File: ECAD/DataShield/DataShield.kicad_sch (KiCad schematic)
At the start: 20 parts, among them J1 RS232, J2 Digital, J3 Conn_01x04, J4 Digital, J5 Analog, J6 Communication, U1 SP213, U3 ST485E

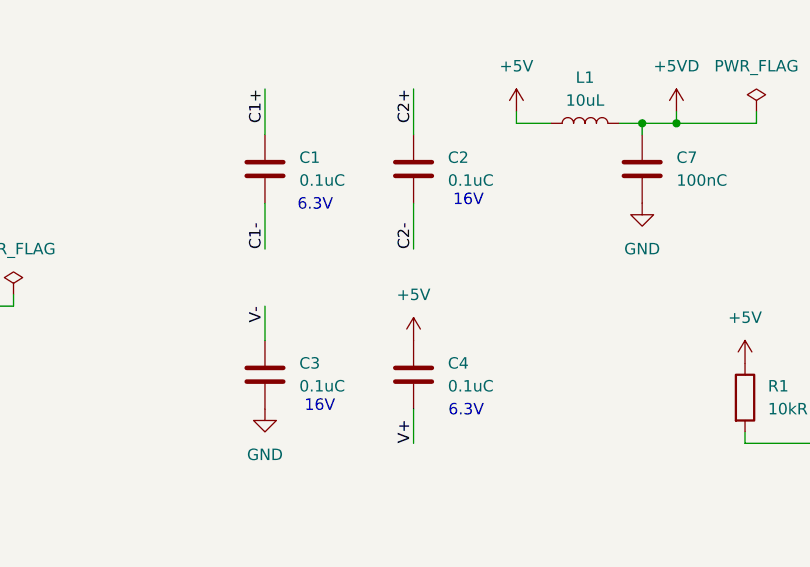
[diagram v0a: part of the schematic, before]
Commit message: Update DataShield.kicad_sch
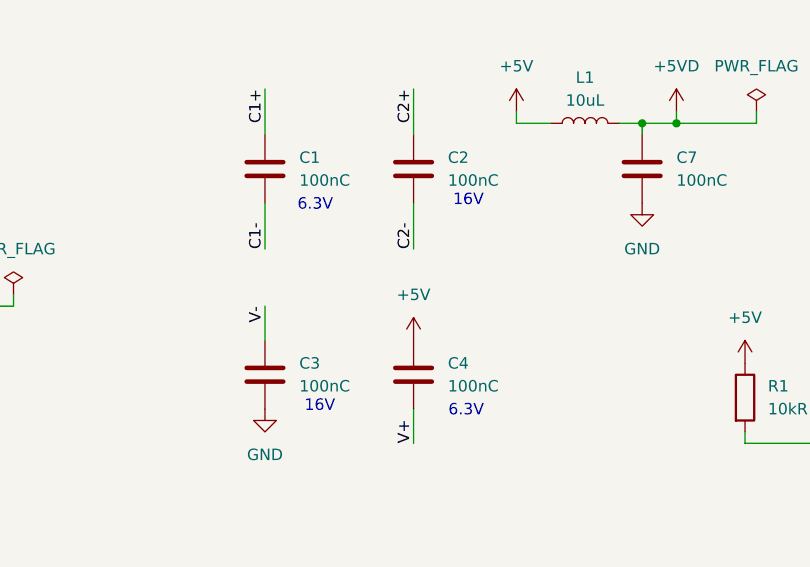
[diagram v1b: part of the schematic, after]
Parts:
- C1, C2, C3, C4: value 0.1uC -> 100nC
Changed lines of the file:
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@@
 			)
 		)
-		(property "Value" "0.1uC"
+		(property "Value" "100nC"
 			(at 123.19 110.4899 0)
 			(effects
@@
 			)
 		)
-		(property "Value" "0.1uC"
+		(property "Value" "100nC"
 			(at 139.7 133.3499 0)
 			(effects
@@
 			)
 		)
-		(property "Value" "0.1uC"
+		(property "Value" "100nC"
 			(at 123.19 133.3499 0)
 			(effects
@@
 			)
 		)
-		(property "Value" "0.1uC"
+		(property "Value" "100nC"
 			(at 139.7 110.4899 0)
 			(effects

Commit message: Progressed ECAD.
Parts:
- C1, C2, C3, C4, C7, C9: MPN (none) -> C0805F104K5RACAUTO; Status (none) -> OK
- R3: value R -> 120R
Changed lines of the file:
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@@
 			)
 		)
-		(property "Value" "R"
+		(property "Value" "120R"
 			(at 226.06 41.9099 0)
 			(effects
@@
 			)
 		)
-		(property "Datasheet" "~"
+		(property "Datasheet" "https://www.lcsc.com/datasheet/lcsc_datasheet_2304140030_KEMET-C0805F104K5RACAUTO_C141162.pdf"
 			(at 161.29 109.22 0)
 			(effects
@@
 			)
 		)
-		(property "Status" ""
+		(property "Status" "OK"
+			(at 161.29 109.22 0)
+			(effects
+				(font
+					(size 1.27 1.27)
+				)
+				(hide yes)
+			)
+		)
+		(property "MPN" "C0805F104K5RACAUTO"
 			(at 161.29 109.22 0)
 			(effects
@@
 			)
 		)
-		(property "Datasheet" "~"
+		(property "Datasheet" "https://www.lcsc.com/datasheet/lcsc_datasheet_2304140030_KEMET-C0805F104K5RACAUTO_C141162.pdf"
 			(at 119.38 109.22 0)
 			(effects
@@
 		)
 		(property "Description" "Unpolarized capacitor"
+			(at 119.38 109.22 0)
+			(effects
+				(font
+					(size 1.27 1.27)
+				)
+				(hide yes)
+			)
+		)
+		(property "MPN" "C0805F104K5RACAUTO"
+			(at 119.38 109.22 0)
+			(effects
+				(font
+					(size 1.27 1.27)
+				)
+				(hide yes)
+			)
+		)
+		(property "Status" "OK"
 			(at 119.38 109.22 0)
 			(effects
@@
 			)
 		)
-		(property "Datasheet" "~"
+		(property "Datasheet" "https://www.lcsc.com/datasheet/lcsc_datasheet_2304140030_KEMET-C0805F104K5RACAUTO_C141162.pdf"
 			(at 135.89 132.08 0)
 			(effects
@@
 		)
 		(property "Description" "Unpolarized capacitor"
+			(at 135.89 132.08 0)
+			(effects
+				(font
+					(size 1.27 1.27)
+				)
+				(hide yes)
+			)
+		)
+		(property "MPN" "C0805F104K5RACAUTO"
+			(at 135.89 132.08 0)
+			(effects
+				(font
+					(size 1.27 1.27)
+				)
+				(hide yes)
+			)
+		)
+		(property "Status" "OK"
 			(at 135.89 132.08 0)
 			(effects
@@
 			)
 		)
-		(property "Datasheet" "~"
+		(property "Datasheet" "https://www.lcsc.com/datasheet/lcsc_datasheet_2304140030_KEMET-C0805F104K5RACAUTO_C141162.pdf"
 			(at 119.38 132.08 0)
 			(effects
@@
 		)
 		(property "Description" "Unpolarized capacitor"
+			(at 119.38 132.08 0)
+			(effects
+				(font
+					(size 1.27 1.27)
+				)
+				(hide yes)
+			)
+		)
+		(property "MPN" "C0805F104K5RACAUTO"
+			(at 119.38 132.08 0)
+			(effects
+				(font
+					(size 1.27 1.27)
+				)
+				(hide yes)
+			)
+		)
+		(property "Status" "OK"
 			(at 119.38 132.08 0)
 			(effects
@@
 			)
 		)
-		(property "Datasheet" "~"
+		(property "Datasheet" "https://www.lcsc.com/datasheet/lcsc_datasheet_2304140030_KEMET-C0805F104K5RACAUTO_C141162.pdf"
 			(at 135.89 109.22 0)
 			(effects
@@
 		)
 		(property "Description" "Unpolarized capacitor"
+			(at 135.89 109.22 0)
+			(effects
+				(font
+					(size 1.27 1.27)
+				)
+				(hide yes)
+			)
+		)
+		(property "MPN" "C0805F104K5RACAUTO"
+			(at 135.89 109.22 0)
+			(effects
+				(font
+					(size 1.27 1.27)
+				)
+				(hide yes)
+			)
+		)
+		(property "Status" "OK"
 			(at 135.89 109.22 0)
 			(effects
@@
 			)
 		)
-		(property "Datasheet" "~"
+		(property "Datasheet" "https://www.lcsc.com/datasheet/lcsc_datasheet_2304140030_KEMET-C0805F104K5RACAUTO_C141162.pdf"
 			(at 161.29 44.45 0)
 			(effects
@@
 			)
 		)
-		(property "Status" ""
+		(property "Status" "OK"
 			(at 161.29 44.45 0)
 			(effects
+				(font
+					(size 1.27 1.27)
+				)
+				(hide yes)
+			)
+		)
+		(property "MPN" "C0805F104K5RACAUTO"
+			(at 161.29 44.45 0)
+			(effects

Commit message: Progressed ECAD.
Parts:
- R1, R2: MPN (none) -> RC0805JR-0710KL; Status (none) -> OK
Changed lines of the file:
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@@
 			)
 		)
-		(property "Datasheet" ""
+		(property "Datasheet" "https://www.lcsc.com/datasheet/lcsc_datasheet_1810171610_YAGEO-RC0805JR-0710KL_C100047.pdf"
 			(at 232.41 134.62 0)
 			(effects
@@
 		)
 		(property "Description" "Resistor"
+			(at 232.41 134.62 0)
+			(effects
+				(font
+					(size 1.27 1.27)
+				)
+				(hide yes)
+			)
+		)
+		(property "MPN" "RC0805JR-0710KL"
+			(at 232.41 134.62 0)
+			(effects
+				(font
+					(size 1.27 1.27)
+				)
+				(hide yes)
+			)
+		)
+		(property "Status" "OK"
 			(at 232.41 134.62 0)
 			(effects
@@
 			)
 		)
-		(property "Datasheet" ""
+		(property "Datasheet" "https://www.lcsc.com/datasheet/lcsc_datasheet_1810171610_YAGEO-RC0805JR-0710KL_C100047.pdf"
 			(at 172.72 134.62 0)
 			(effects
@@
 			(at 172.72 134.62 0)
 			(effects
+				(font
+					(size 1.27 1.27)
+				)
+				(hide yes)
+			)
+		)
+		(property "MPN" "RC0805JR-0710KL"
+			(at 172.72 134.62 0)
+			(effects
+				(font
+					(size 1.27 1.27)
+				)
+				(hide yes)
+			)
+		)
+		(property "Status" "OK"
+			(at 172.72 134.62 0)
+			(effects

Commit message: Progressed ECAD.
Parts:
- removed J3: Conn_01x04, Connector_JST:JST_EH_B4B-EH-A_1x04_P2.50mm_Vertical, symbol Connector_Generic:Conn_01x04
- added J7: Conn_02x03_Odd_Even, Connector_IDC:IDC-Header_2x03_P2.54mm_Vertical, symbol Connector_Generic:Conn_02x03_Odd_Even
- R3: footprint (none) -> Resistor_SMD:R_1206_3216Metric; MPN (none) -> RC1206FR-7W120RL; Status (none) -> OK
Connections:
- net GND: now also J7.3 (Pin_3), J7.4 (Pin_4)
- net at R3.1, U3.6 (A): now also J7.2 (Pin_2)
- net at R3.2, U3.7 (B): now also J7.1 (Pin_1)
- no-connect marks 13 -> 15
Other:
- moved on the sheet: R3

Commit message: Progressed ECAD.
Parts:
- removed R3: 120R, Resistor_SMD:R_1206_3216Metric, symbol Device:R
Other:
- moved on the sheet: J7
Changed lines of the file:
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@@
 	)
 	(junction
-		(at 233.68 48.26)
-		(diameter 0)
-		(color 0 0 0 0)
-	)
-	(junction
 		(at 165.1 104.14)
 		(diameter 0)
@@
 	)
 	(junction
-		(at 233.68 33.02)
-		(diameter 0)
-		(color 0 0 0 0)
-	)
-	(junction
 		(at 83.82 124.46)
 		(diameter 0)
@@
 	)
 	(no_connect
-		(at 250.19 34.29)
+		(at 228.6 34.29)
 	)
 	(no_connect
@@
 	)
 	(no_connect
-		(at 250.19 46.99)
+		(at 228.6 46.99)
 	)
 	(no_connect
@@
 	(wire
 		(pts
-			(xy 219.71 33.02) (xy 233.68 33.02)
-		)
-		(stroke
-			(width 0)
-			(type default)
-		)
-	)
-	(wire
-		(pts
 			(xy 196.85 128.27) (xy 187.96 128.27)
 		)
@@
 	(wire
 		(pts
-			(xy 245.11 48.26) (xy 233.68 48.26)
-		)
-		(stroke
-			(width 0)
-			(type default)
-		)
-	)
-	(wire
-		(pts
 			(xy 184.15 40.64) (xy 196.85 40.64)
 		)
@@
 	(wire
 		(pts
-			(xy 219.71 48.26) (xy 233.68 48.26)
+			(xy 219.71 48.26) (xy 223.52 48.26)
 		)
 		(stroke
@@
 	(wire
 		(pts
-			(xy 245.11 33.02) (xy 233.68 33.02)
+			(xy 219.71 33.02) (xy 223.52 33.02)
 		)
 		(stroke
@@
 	(wire
 		(pts
-			(xy 245.11 34.29) (xy 245.11 33.02)
+			(xy 223.52 34.29) (xy 223.52 33.02)
 		)
 		(stroke
@@
 	(wire
 		(pts
-			(xy 245.11 46.99) (xy 245.11 48.26)
+			(xy 223.52 46.99) (xy 223.52 48.26)
 		)
 		(stroke
@@
 	(wire
 		(pts
-			(xy 233.68 33.02) (xy 233.68 36.83)
-		)
-		(stroke
-			(width 0)
-			(type default)
-		)
-	)
-	(wire
-		(pts
 			(xy 196.85 133.35) (xy 187.96 133.35)
 		)
@@
 	(wire
 		(pts
-			(xy 233.68 44.45) (xy 233.68 48.26)
-		)
-		(stroke
-			(width 0)
-			(type default)
-		)
-	)
-	(wire
-		(pts
 			(xy 147.32 39.37) (xy 151.13 39.37)
 		)
@@
 	)
 	(symbol
-		(lib_id "Device:R")
-		(at 233.68 40.64 0)
-		(unit 1)
-		(exclude_from_sim no)
-		(in_bom yes)
-		(on_board yes)
-		(dnp no)
-		(fields_autoplaced yes)
-		(property "Reference" "R3"
-			(at 236.22 39.3699 0)
-			(effects
-				(font
-					(size 1.27 1.27)
-				)
-				(justify left)
-			)
-		)
-		(property "Value" "120R"
-			(at 236.22 41.9099 0)
-			(effects
-				(font
-					(size 1.27 1.27)
-				)
-				(justify left)
-			)
-		)
-		(property "Footprint" "Resistor_SMD:R_1206_3216Metric"
-			(at 231.902 40.64 90)
-			(effects
-				(font
-					(size 1.27 1.27)
-				)
-				(hide yes)
-			)
-		)
-		(property "Datasheet" "https://www.lcsc.com/datasheet/lcsc_datasheet_2011202108_YAGEO-RC1206FR-7W120RL_C914848.pdf"
-			(at 233.68 40.64 0)
-			(effects
-				(font
-					(size 1.27 1.27)
-				)
-				(hide yes)
-			)
-		)
-		(property "Description" "Resistor"
-			(at 233.68 40.64 0)
-			(effects
-				(font
-					(size 1.27 1.27)
-				)
-				(hide yes)
-			)
-		)
-		(property "MPN" "RC1206FR-7W120RL"
-			(at 233.68 40.64 0)
-			(effects
-				(font
-					(size 1.27 1.27)
-				)
-				(hide yes)
-			)
-		)
-		(property "Status" "OK"
-			(at 233.68 40.64 0)
-			(effects
-				(font
-					(size 1.27 1.27)
-				)
-				(hide yes)
-			)
-		)
-		(pin "2"
-		)
-		(pin "1"
-		)
-		(instances
-			(project "DataShield"
-				(path "/e63e39d7-6ac0-4ffd-8aa3-1841a4541b55"
-					(reference "R3")
-					(unit 1)
-				)
-			)
-		)
-	)
-	(symbol
 		(lib_id "Connector_Generic:Conn_01x02")
 		(at 35.56 135.89 0)
@@
 		(lib_name "GND_2")
 		(lib_id "power:GND")
-		(at 247.65 46.99 0)
+		(at 226.06 46.99 0)
 		(unit 1)
 		(exclude_from_sim no)
@@
 		(fields_autoplaced yes)
 		(property "Reference" "#PWR019"
-			(at 247.65 53.34 0)
+			(at 226.06 53.34 0)
 			(effects
 				(font
@@
 		)
 		(property "Value" "GND"
-			(at 247.65 52.07 0)
+			(at 226.06 52.07 0)
 			(effects
 				(font
@@
 		)
 		(property "Footprint" ""
-			(at 247.65 46.99 0)
+			(at 226.06 46.99 0)
 			(effects
 				(font
@@
 		)
 		(property "Datasheet" ""
-			(at 247.65 46.99 0)
+			(at 226.06 46.99 0)
 			(effects
 				(font
@@
 		)
 		(property "Description" "Power symbol creates a global label with name \"GND\" , ground"
-			(at 247.65 46.99 0)
+			(at 226.06 46.99 0)
 			(effects
 				(font
@@
 	(symbol
 		(lib_id "Connector_Generic:Conn_02x03_Odd_Even")
-		(at 247.65 41.91 90)
+		(at 226.06 41.91 90)
 		(unit 1)
 		(exclude_from_sim no)
@@
 		(fields_autoplaced yes)
 		(property "Reference" "J7"
-			(at 252.73 39.3699 90)
+			(at 231.14 39.3699 90)
 			(effects
 				(font
@@
 		)
 		(property "Value" "Conn_02x03_Odd_Even"
-			(at 252.73 41.9099 90)
+			(at 231.14 41.9099 90)
 			(effects
 				(font
@@
 		)
 		(property "Footprint" "Connector_IDC:IDC-Header_2x03_P2.54mm_Vertical"
-			(at 247.65 41.91 0)
+			(at 226.06 41.91 0)
 			(effects
 				(font
@@
 		)
 		(property "Datasheet" "https://www.lcsc.com/datasheet/lcsc_datasheet_2303141000_HCTL-HC-JN254-2-03-Z_C5372863.pdf"
-			(at 247.65 41.91 0)
+			(at 226.06 41.91 0)
 			(effects
 				(font
@@
 		)
 		(property "Description" "Generic connector, double row, 02x03, odd/even pin numbering scheme (row 1 odd numbers, row 2 even numbers), script generated (kicad-library-utils/schlib/autogen/connector/)"
-			(at 247.65 41.91 0)
+			(at 226.06 41.91 0)
 			(effects
 				(font
@@
 		)
 		(property "MPN" "HC-JN254-2-03-Z"
-			(at 247.65 41.91 0)
+			(at 226.06 41.91 0)
 			(effects
 				(font
@@
 		)
 		(property "Status" "OK"
-			(at 247.65 41.91 0)
+			(at 226.06 41.91 0)
 			(effects
 				(font
@@
 		(lib_name "GND_2")
 		(lib_id "power:GND")
-		(at 247.65 34.29 180)
+		(at 226.06 34.29 180)
 		(unit 1)
 		(exclude_from_sim no)
@@
 		(fields_autoplaced yes)
 		(property "Reference" "#PWR08"
-			(at 247.65 27.94 0)
+			(at 226.06 27.94 0)
 			(effects
 				(font
@@
 		)
 		(property "Value" "GND"
-			(at 247.65 29.21 0)
+			(at 226.06 29.21 0)
 			(effects
 				(font
@@
 		)
 		(property "Footprint" ""
-			(at 247.65 34.29 0)
+			(at 226.06 34.29 0)
 			(effects
 				(font
@@
 		)
 		(property "Datasheet" ""
-			(at 247.65 34.29 0)
+			(at 226.06 34.29 0)
 			(effects
 				(font
@@
 		)
 		(property "Description" "Power symbol creates a global label with name \"GND\" , ground"
-			(at 247.65 34.29 0)
+			(at 226.06 34.29 0)
 			(effects
 				(font

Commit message: Progressed ECAD.
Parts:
- removed C8: 100uC, Capacitor_SMD:CP_Elec_6.3x5.4_Nichicon, symbol Device:C_Polarized
- added C5: 10uC, Capacitor_SMD:C_1206_3216Metric, symbol Device:C
- added J3: Wire RS485, Connector_IDC:IDC-Header_2x03_P2.54mm_Vertical, symbol Connector_Generic:Conn_02x03_Odd_Even
- J7: value Conn_02x03_Odd_Even -> RS485
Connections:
- net +5V: now also C5.1
- net GND: now also C5.2

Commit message: Progressed ECAD.
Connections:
- net 22: no longer U1.5 (ROUT2)
- net 23: no longer U1.26 (ROUT3)
- net 24: no longer U1.22 (ROUT4)
- net 25: no longer U1.19 (ROUT5)
- net A12: now also U1.5 (ROUT2)
- net A13: now also U1.26 (ROUT3)
- net A14: now also U1.22 (ROUT4)
- net A15: now also U1.19 (ROUT5)
- no-connect marks 15 -> 21
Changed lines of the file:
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@@
 	)
 	(no_connect
-		(at 29.21 64.77)
+		(at 76.2 120.65)
 	)
 	(no_connect
@@
 	)
 	(no_connect
+		(at 245.11 46.99)
+	)
+	(no_connect
 		(at 85.09 69.85)
 	)
 	(no_connect
+		(at 247.65 34.29)
+	)
+	(no_connect
+		(at 73.66 153.67)
+	)
+	(no_connect
 		(at 228.6 46.99)
 	)
@@
 	)
 	(no_connect
-		(at 29.21 72.39)
+		(at 76.2 153.67)
+	)
+	(no_connect
+		(at 247.65 46.99)
 	)
 	(no_connect
@@
 	)
 	(no_connect
-		(at 29.21 67.31)
+		(at 242.57 34.29)
+	)
+	(no_connect
+		(at 245.11 34.29)
 	)
 	(no_connect
@@
 	)
 	(no_connect
-		(at 29.21 69.85)
+		(at 242.57 46.99)
+	)
+	(no_connect
+		(at 73.66 120.65)
 	)
 	(no_connect
@@
 	(wire
 		(pts
+			(xy 30.48 64.77) (xy 43.18 64.77)
+		)
+		(stroke
+			(width 0)
+			(type default)
+		)
+	)
+	(wire
+		(pts
 			(xy 71.12 59.69) (xy 83.82 59.69)
 		)
@@
 	(wire
 		(pts
-			(xy 29.21 72.39) (xy 43.18 72.39)
-		)
-		(stroke
-			(width 0)
-			(type solid)
-		)
-	)
-	(wire
-		(pts
 			(xy 83.82 123.19) (xy 83.82 124.46)
 		)
@@
 	(wire
 		(pts
-			(xy 43.18 69.85) (xy 29.21 69.85)
+			(xy 29.21 133.35) (xy 29.21 135.89)
 		)
 		(stroke
 			(width 0)
-			(type solid)
+			(type default)
 		)
 	)
 	(wire
 		(pts
-			(xy 29.21 133.35) (xy 29.21 135.89)
+			(xy 29.21 135.89) (xy 29.21 138.43)
 		)
 		(stroke
@@
 	(wire
 		(pts
-			(xy 29.21 135.89) (xy 29.21 138.43)
+			(xy 184.15 45.72) (xy 196.85 45.72)
 		)
 		(stroke
 			(width 0)
-			(type default)
+			(type solid)
 		)
 	)
 	(wire
 		(pts
-			(xy 184.15 45.72) (xy 196.85 45.72)
+			(xy 71.12 67.31) (xy 83.82 67.31)
 		)
 		(stroke
@@
 	(wire
 		(pts
-			(xy 71.12 67.31) (xy 83.82 67.31)
+			(xy 30.48 69.85) (xy 43.18 69.85)
 		)
 		(stroke
 			(width 0)
-			(type solid)
+			(type default)
 		)
 	)
@@
 	(wire
 		(pts
+			(xy 30.48 67.31) (xy 43.18 67.31)
+		)
+		(stroke
+			(width 0)
+			(type default)
+		)
+	)
+	(wire
+		(pts
 			(xy 196.85 135.89) (xy 187.96 135.89)
 		)
@@
 	(wire
 		(pts
-			(xy 29.21 67.31) (xy 43.18 67.31)
-		)
-		(stroke
-			(width 0)
-			(type solid)
-		)
-	)
-	(wire
-		(pts
 			(xy 219.71 33.02) (xy 219.71 38.1)
 		)
@@
 	(wire
 		(pts
-			(xy 147.32 39.37) (xy 151.13 39.37)
+			(xy 30.48 72.39) (xy 43.18 72.39)
 		)
 		(stroke
@@
 	(wire
 		(pts
-			(xy 196.85 119.38) (xy 187.96 119.38)
+			(xy 147.32 39.37) (xy 151.13 39.37)
 		)
 		(stroke
 			(width 0)
-			(type solid)
+			(type default)
 		)
 	)
 	(wire
 		(pts
-			(xy 184.15 50.8) (xy 196.85 50.8)
+			(xy 196.85 119.38) (xy 187.96 119.38)
 		)
 		(stroke
@@
 	(wire
 		(pts
-			(xy 43.18 64.77) (xy 29.21 64.77)
+			(xy 184.15 50.8) (xy 196.85 50.8)
 		)
 		(stroke
@@
 		)
 	)
-	(label "RX2{slash}17"
-		(at 184.15 40.64 0)
+	(label "A14"
+		(at 187.96 133.35 0)
 		(fields_autoplaced yes)
 		(effects
@@
 		)
 	)
-	(label "25"
-		(at 73.66 153.67 90)
+	(label "RX2{slash}17"
+		(at 184.15 40.64 0)
 		(fields_autoplaced yes)
 		(effects
@@
 		)
 	)
-	(label "DCD"
-		(at 248.92 109.22 0)
+	(label "25"
+		(at 73.66 153.67 90)
 		(fields_autoplaced yes)
 		(effects
@@
 		)
 	)
-	(label "22"
-		(at 187.96 128.27 0)
+	(label "DCD"
+		(at 248.92 109.22 0)
 		(fields_autoplaced yes)
 		(effects
@@
 		)
 	)
+	(label "A12"
+		(at 187.96 128.27 0)
+		(fields_autoplaced yes)
+		(effects
+			(font
+				(size 1.27 1.27)
+			)
+			(justify left bottom)
+		)
+	)
 	(label "23"
 		(at 76.2 153.67 90)
@@
 		)
 	)
-	(label "TX1{slash}18"
-		(at 184.15 43.18 0)
+	(label "A13"
+		(at 187.96 130.81 0)
 		(fields_autoplaced yes)
 		(effects
@@
 		)
 	)
-	(label "23"
-		(at 187.96 130.81 0)
+	(label "TX1{slash}18"
+		(at 184.15 43.18 0)
 		(fields_autoplaced yes)
 		(effects
@@
 		)
 	)
+	(label "A15"
+		(at 187.96 135.89 0)
+		(fields_autoplaced yes)
+		(effects
+			(font
+				(size 1.27 1.27)
+			)
+			(justify left bottom)
+		)
+	)
 	(label "RX1{slash}19"
 		(at 83.82 67.31 180)
@@
 		)
 	)
-	(label "24"
-		(at 187.96 133.35 0)
-		(fields_autoplaced yes)
-		(effects
-			(font
-				(size 1.27 1.27)
-			)
-			(justify left bottom)
-		)
-	)
 	(label "RI"
 		(at 248.92 127 0)
@@
 		)
 	)
-	(label "25"
-		(at 187.96 135.89 0)
-		(fields_autoplaced yes)
-		(effects
-			(font
-				(size 1.27 1.27)
-			)
-			(justify left bottom)
-		)
-	)
 	(label "C1-"
 		(at 187.96 104.14 0)
@@
 		(exclude_from_sim no)
 		(in_bom yes)
-		(on_board yes)
+		(on_board no)
 		(dnp yes)
 		(fields_autoplaced yes)

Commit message: Progressed ECAD.
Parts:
- added C6: 100nC, Capacitor_SMD:C_0805_2012Metric, symbol Device:C
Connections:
- net +5V: now also C6.1
- net 26: no longer U1.6 (DIN2)
- net 27: no longer U1.20 (DIN3)
- net A10: now also U1.6 (DIN2)
- net A11: now also U1.20 (DIN3)
- net A8: now also U3.2 (~{RE})
- net A9: now also U3.3 (DE)
- net GND: now also C6.2
- net RX1/19: no longer U3.3 (DE)
- net TX1/18: no longer U3.2 (~{RE})
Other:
- note added: "Power supply decoupling"
- moved on the sheet: C5, J2, J4, J5, J6
